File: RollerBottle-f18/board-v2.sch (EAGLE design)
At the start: 23 parts, among them IC1 7805T, J1 POWER_JACKPTH_BREAD, U1 328P

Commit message: Updated Big easy stepper design block and added to board_v2
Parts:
- removed INPUT: (no value), pinhead:PINHD-1X10
- removed MOTOR: (no value), pinhead:PINHD-1X4
- removed POWER: (no value), pinhead:PINHD-1X2
- added JP4: (no value), pinhead:PINHD-1X10
- added JP5: (no value), pinhead:PINHD-1X2
- added JP6: (no value), pinhead:PINHD-1X4
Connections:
- removed net N$10: A1-2.K, MOTOR.2
- removed net N$11: A1-3.K, MOTOR.3
- removed net N$12: A1-4.K, MOTOR.4
- removed net N$9: A1-1.K, MOTOR.1
- new net M_+12V: JP5.1
- new net M_A+: A1-4.K, JP6.4
- new net M_A-: A1-3.K, JP6.3
- new net M_B+: A1-1.K, JP6.1
- new net M_B-: A1-2.K, JP6.2
- new net M_DIR: JP4.1
- new net M_ENABLE: JP4.10
- new net M_GND: JP4.3, JP5.2
- new net M_MS1: JP4.9
- new net M_MS2: JP4.8
- new net M_MS3: JP4.7
- new net M_RST: JP4.6
- new net M_SLEEP: JP4.5
- new net M_STEP: JP4.2
- new net M_VCC: JP4.4
- net +12V: no longer POWER.2
- net GND: no longer INPUT.3, POWER.1
- net STEP: no longer INPUT.2
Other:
- note added: "Motor Output"
- note added: "Stepper Motor Controller"
- moved on the sheet: A1-1, A1-2, A1-3, A1-4

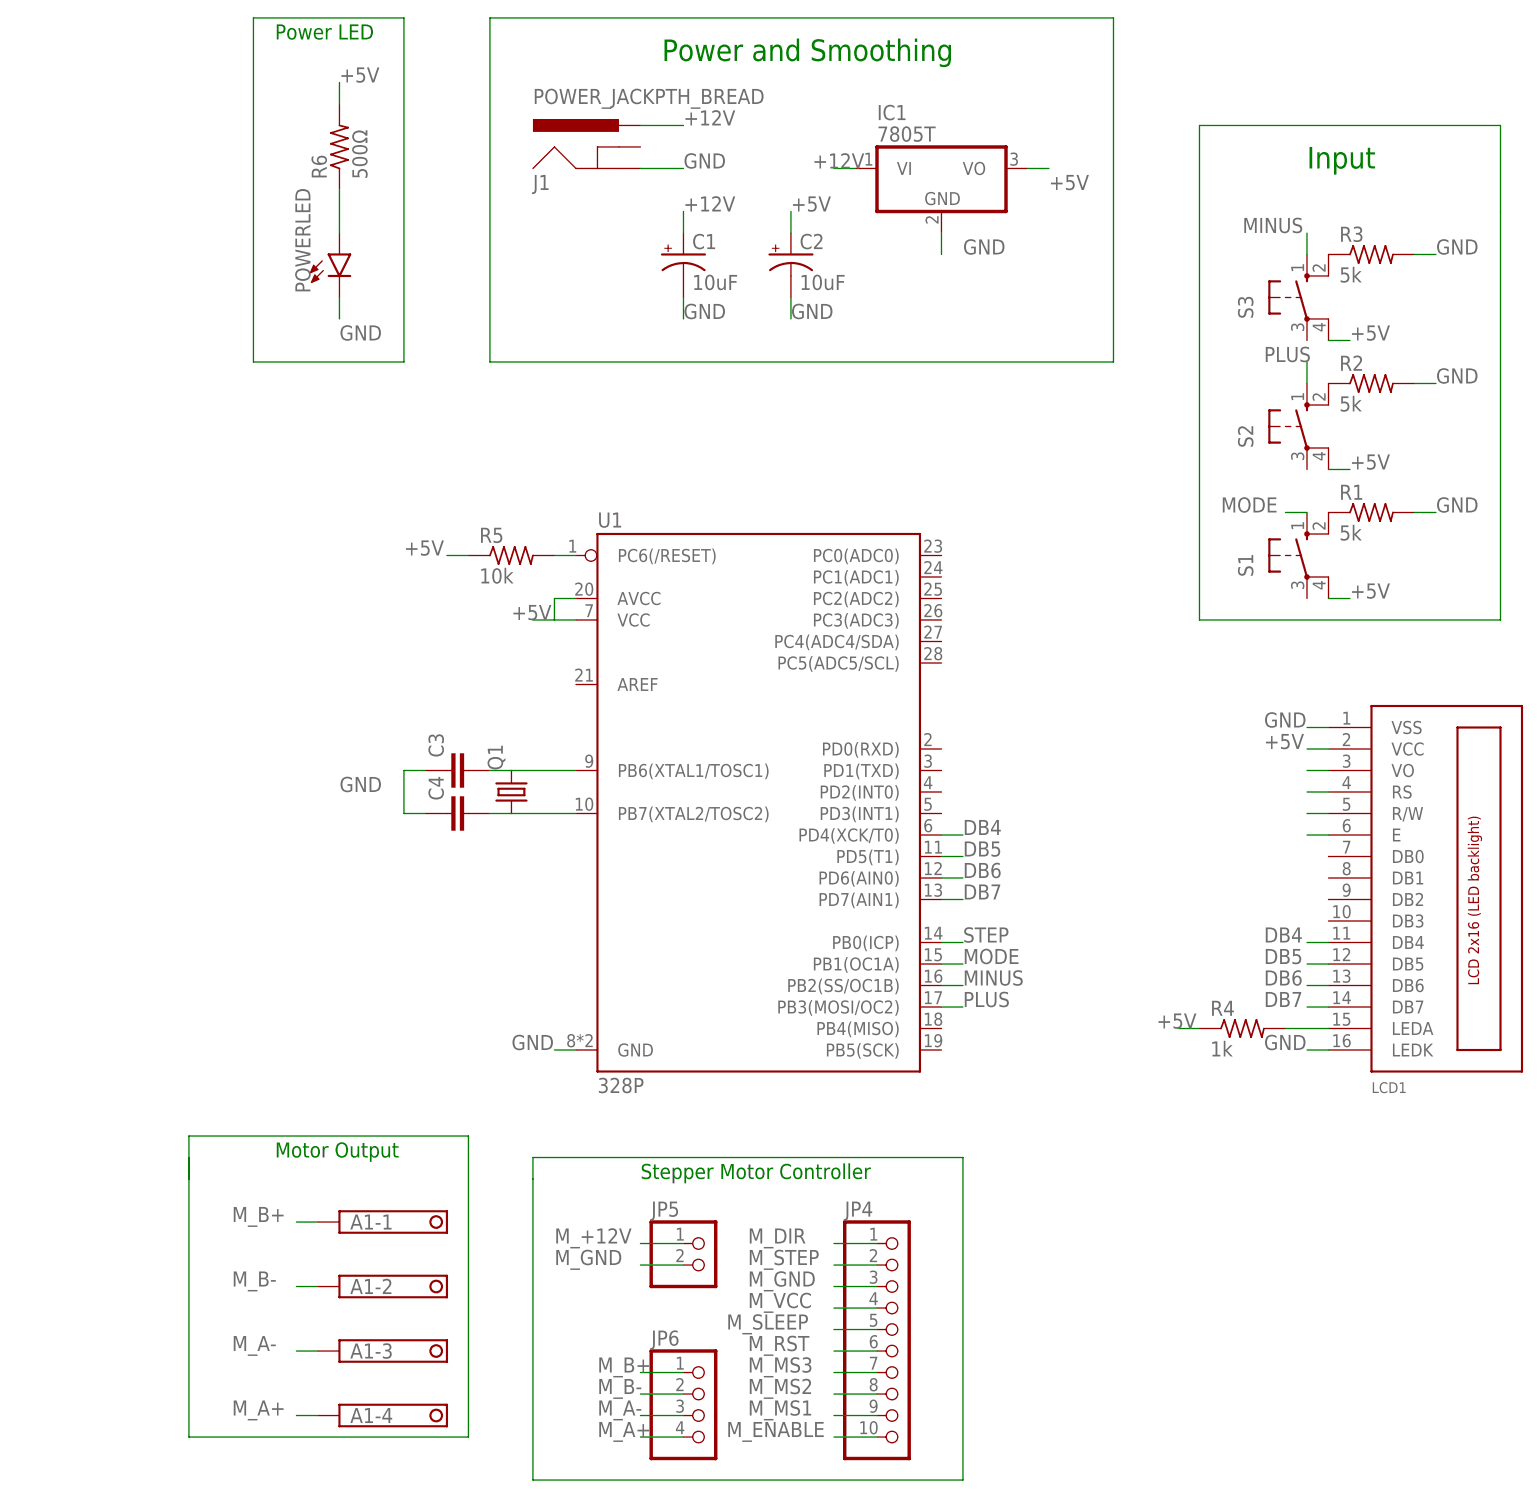
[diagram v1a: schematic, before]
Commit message: Traces added
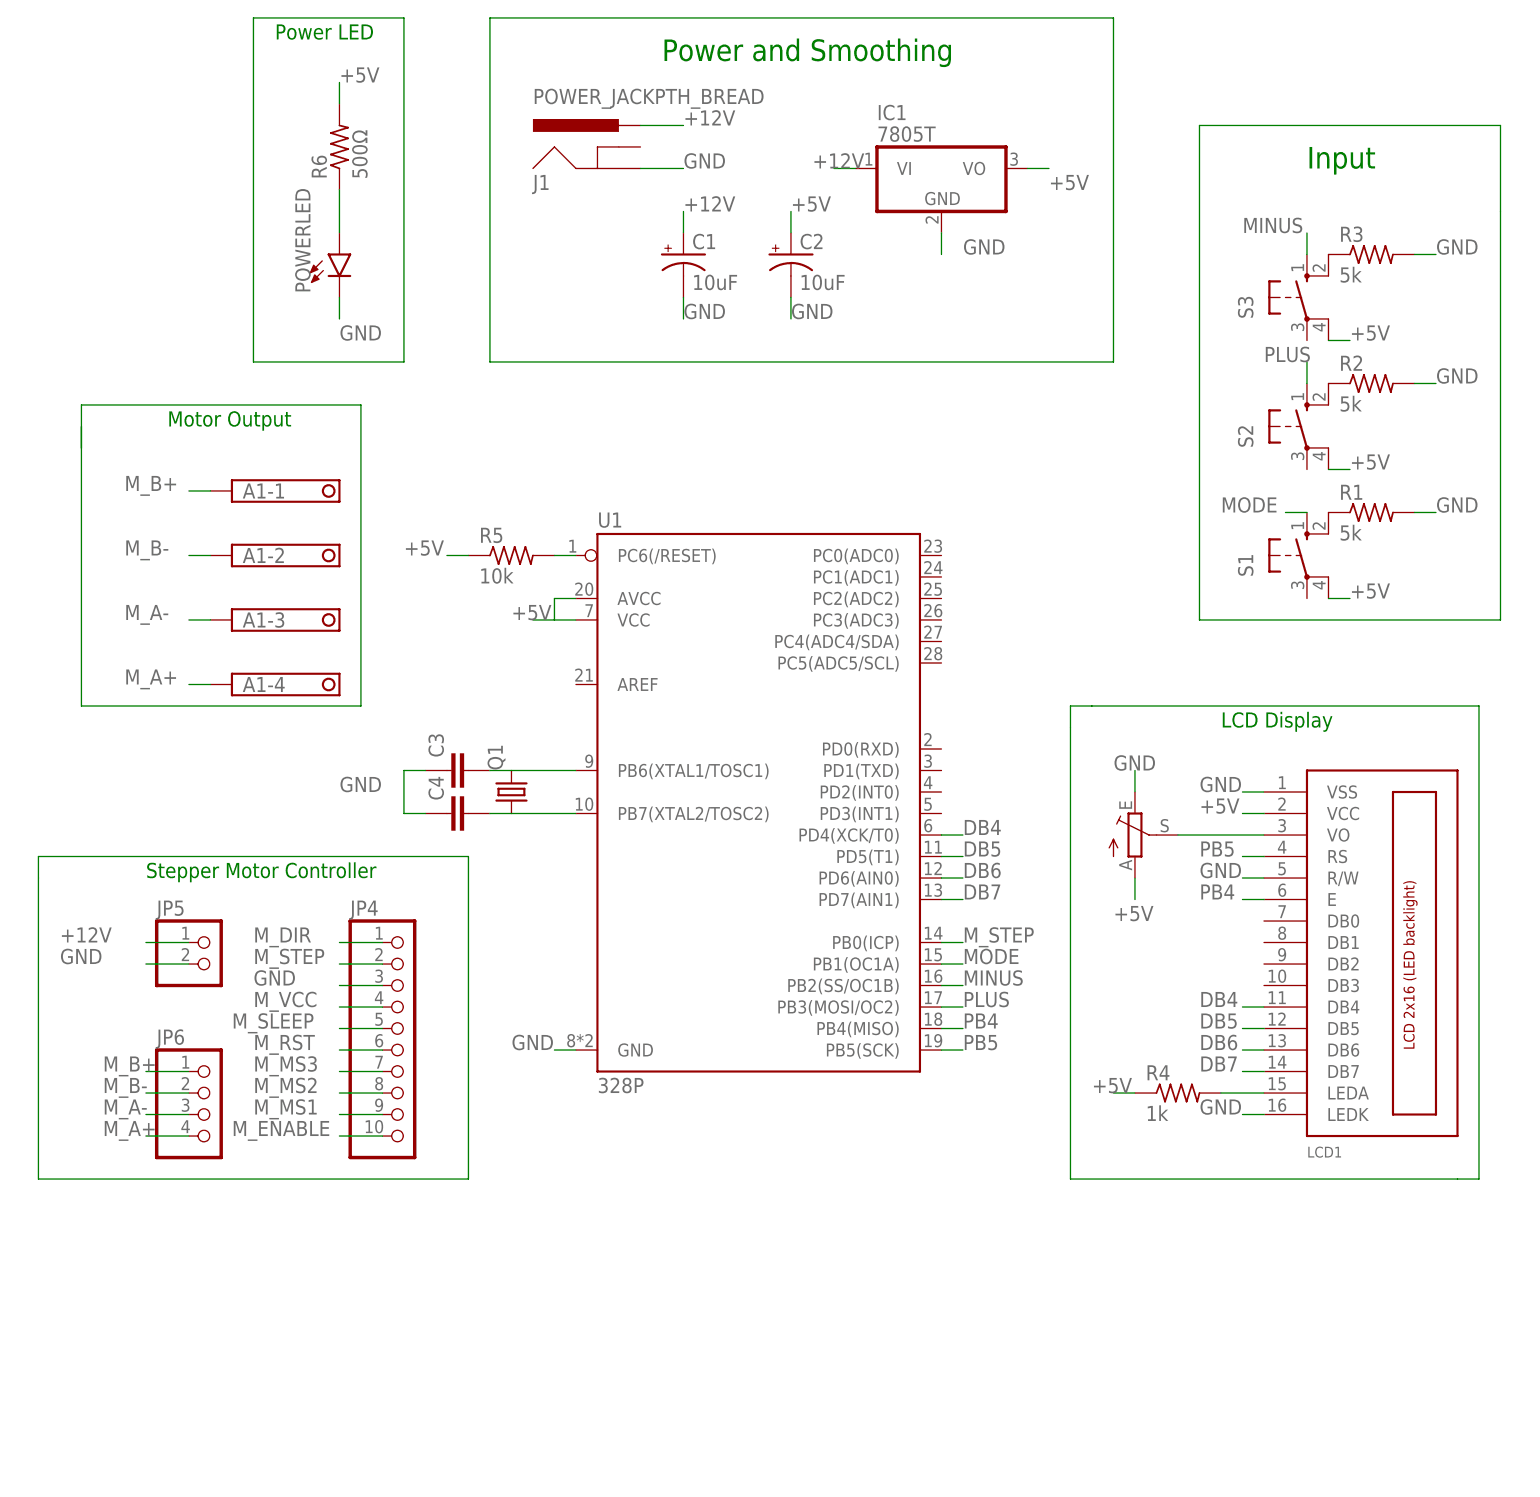
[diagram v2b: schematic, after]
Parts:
- added R7: (no value), pot:TRIM_EU-S63S
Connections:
- removed net M_+12V: JP5.1
- removed net M_GND: JP4.3, JP5.2
- removed net N$5: LCD1.RS
- removed net N$6: LCD1.R/W
- removed net N$7: LCD1.E
- removed net STEP: U1.PB0(ICP)
- new net PB4: LCD1.E, U1.PB4(MISO)
- new net PB5: LCD1.RS, U1.PB5(SCK)
- net +12V: now also JP5.1
- net +5V: now also R7.A
- net GND: now also JP4.3, JP5.2, LCD1.R/W, R7.E
- net M_STEP: now also U1.PB0(ICP)
- net N$2: now also R7.S
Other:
- note added: "LCD Display"
- moved on the sheet: A1-1, A1-2, A1-3, A1-4, JP4, JP5, JP6, LCD1, R4

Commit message: Backing up board v2
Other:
- note added: "Drew Applegath 10/16/2018 Board-v2"
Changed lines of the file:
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@@
 <text x="-68.58" y="40.64" size="1.778" layer="91">Motor Output</text>
 <text x="55.88" y="5.08" size="1.778" layer="91">LCD Display</text>
+<text x="-5.08" y="-66.04" size="1.778" layer="91" font="vector">Drew Applegath
+10/16/2018
+Board-v2</text>
 </plain>
 <instances>
@@
 </drawing>
 <compatibility>
+<note version="6.3" minversion="6.2.2" severity="warning">
+Since Version 6.2.2 text objects can contain more than one line,
+which will not be processed correctly with this version.
+</note>
 <note version="8.2" severity="warning">
 Since Version 8.2, EAGLE supports online libraries. The ids
